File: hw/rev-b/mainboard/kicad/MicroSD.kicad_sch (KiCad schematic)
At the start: 5 parts, among them J25 MICRO_SD

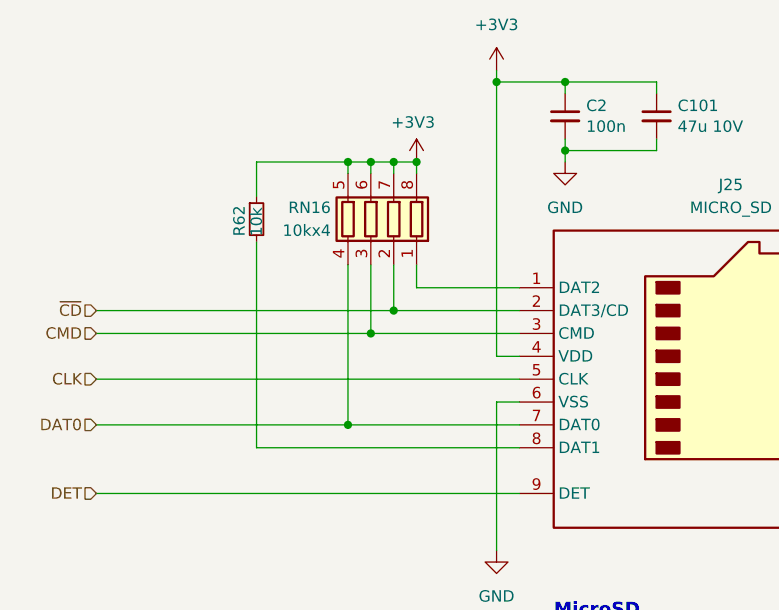
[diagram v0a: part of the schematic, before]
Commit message: hw: move USB-C for 8032SK (WIP)
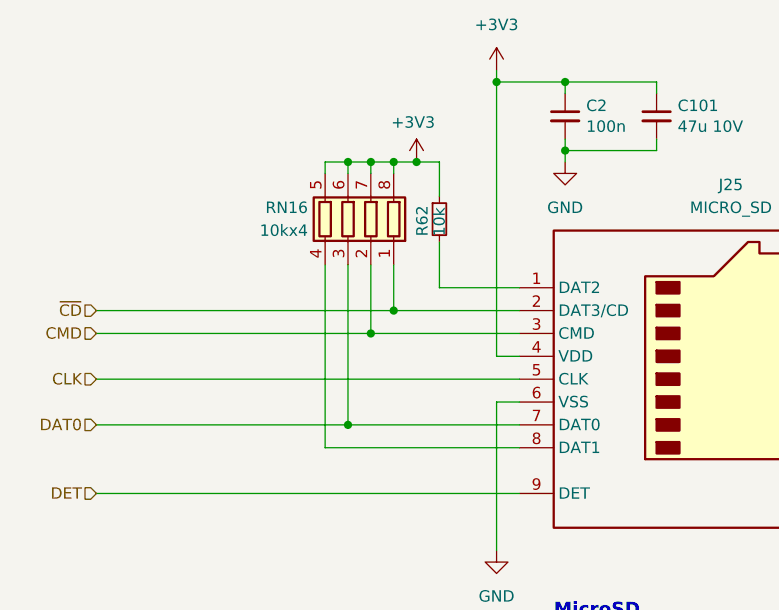
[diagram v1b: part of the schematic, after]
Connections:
- net CMD: now also RN16.2 (R2.1); no longer RN16.3 (R3.1)
- net DAT0: now also RN16.3 (R3.1); no longer RN16.4 (R4.1)
- net ~{CD}: now also RN16.1 (R1.1); no longer RN16.2 (R2.1)
- net at J25.1 (DAT2): now also R62.2; no longer RN16.1 (R1.1)
- net at J25.8 (DAT1): now also RN16.4 (R4.1); no longer R62.2
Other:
- moved on the sheet: R62, RN16
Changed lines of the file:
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@@
 	(wire
 		(pts
-			(xy 120.65 106.68) (xy 149.86 106.68)
-		)
-		(stroke
-			(width 0)
-			(type default)
-		)
-	)
-	(wire
-		(pts
-			(xy 120.65 74.93) (xy 130.81 74.93)
+			(xy 128.27 74.93) (xy 130.81 74.93)
 		)
 		(stroke
@@
 	(wire
 		(pts
+			(xy 128.27 74.93) (xy 128.27 76.2)
+		)
+		(stroke
+			(width 0)
+			(type default)
+		)
+	)
+	(wire
+		(pts
 			(xy 154.94 73.66) (xy 154.94 72.39)
 		)
@@
 	(wire
 		(pts
-			(xy 149.86 88.9) (xy 138.43 88.9)
+			(xy 149.86 88.9) (xy 140.97 88.9)
 		)
 		(stroke
@@
 	(wire
 		(pts
-			(xy 120.65 78.74) (xy 120.65 74.93)
+			(xy 128.27 106.68) (xy 149.86 106.68)
 		)
 		(stroke
@@
 	(wire
 		(pts
+			(xy 140.97 78.74) (xy 140.97 74.93)
+		)
+		(stroke
+			(width 0)
+			(type default)
+		)
+	)
+	(wire
+		(pts
 			(xy 135.89 86.36) (xy 135.89 91.44)
 		)
@@
 	(wire
 		(pts
-			(xy 138.43 74.93) (xy 138.43 76.2)
+			(xy 140.97 74.93) (xy 138.43 74.93)
 		)
 		(stroke
@@
 	(wire
 		(pts
+			(xy 140.97 83.82) (xy 140.97 88.9)
+		)
+		(stroke
+			(width 0)
+			(type default)
+		)
+	)
+	(wire
+		(pts
 			(xy 133.35 93.98) (xy 149.86 93.98)
 		)
@@
 	(wire
 		(pts
-			(xy 120.65 106.68) (xy 120.65 83.82)
-		)
-		(stroke
-			(width 0)
-			(type default)
-		)
-	)
-	(wire
-		(pts
 			(xy 102.87 93.98) (xy 133.35 93.98)
 		)
@@
 	(wire
 		(pts
-			(xy 138.43 86.36) (xy 138.43 88.9)
-		)
-		(stroke
-			(width 0)
-			(type default)
-		)
-	)
-	(wire
-		(pts
 			(xy 135.89 74.93) (xy 135.89 76.2)
 		)
@@
 		(pts
 			(xy 154.94 66.04) (xy 165.1 66.04)
+		)
+		(stroke
+			(width 0)
+			(type default)
+		)
+	)
+	(wire
+		(pts
+			(xy 128.27 86.36) (xy 128.27 106.68)
 		)
 		(stroke
@@
 	(symbol
 		(lib_id "Device:R_Pack04")
-		(at 133.35 81.28 0)
+		(at 130.81 81.28 0)
 		(mirror y)
 		(unit 1)
@@
 		(dnp no)
 		(property "Reference" "RN16"
-			(at 128.905 80.01 0)
+			(at 126.365 80.01 0)
 			(effects
 				(font
@@
 		)
 		(property "Value" "10kx4"
-			(at 128.905 82.55 0)
+			(at 126.365 82.55 0)
 			(effects
 				(font
@@
 		)
 		(property "Footprint" "Resistor_SMD:R_Array_Convex_4x0603"
-			(at 126.365 81.28 90)
+			(at 123.825 81.28 90)
 			(effects
 				(font
@@
 		)
 		(property "Datasheet" "https://www.lcsc.com/datasheet/lcsc_datasheet_2304140030_UNI-ROYAL-Uniroyal-Elec-4D03WGJ0103T5E_C29718.pdf"
-			(at 133.35 81.28 0)
+			(at 130.81 81.28 0)
 			(effects
 				(font
@@
 		)
 		(property "Description" "4 resistor network, parallel topology"
-			(at 133.35 81.28 0)
+			(at 130.81 81.28 0)
 			(effects
 				(font
@@
 		)
 		(property "LCSC" "C29718"
-			(at 133.35 81.28 0)
+			(at 130.81 81.28 0)
 			(effects
 				(font
@@
 	(symbol
 		(lib_id "Device:R_Small")
-		(at 120.65 81.28 0)
+		(at 140.97 81.28 0)
 		(unit 1)
 		(exclude_from_sim no)
@@
 		(dnp no)
 		(property "Reference" "R62"
-			(at 118.745 83.185 90)
+			(at 139.065 83.185 90)
 			(effects
 				(font
@@
 		)
 		(property "Value" "10k"
-			(at 120.65 83.185 90)
+			(at 140.97 83.185 90)
 			(effects
 				(font
@@
 		)
 		(property "Footprint" "Resistor_SMD:R_0402_1005Metric"
-			(at 120.65 81.28 0)
+			(at 140.97 81.28 0)
 			(effects
 				(font
@@
 		)
 		(property "Datasheet" "https://jlcpcb.com/api/file/downloadByFileSystemAccessId/8556212101498380288"
-			(at 120.65 81.28 0)
+			(at 140.97 81.28 0)
 			(effects
 				(font
@@
 		)
 		(property "Description" ""
-			(at 120.65 81.28 0)
+			(at 140.97 81.28 0)
 			(effects
 				(font
@@
 		)
 		(property "LCSC" "C25744"
-			(at 120.65 81.28 0)
-			(effects
-				(font
+			(at 140.97 81.28 0)
+			(effects
+				(font

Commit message: chore(hw): tidy and set ${REVISION} to "B"
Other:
- company: https://is.gd/6hpvh6 -> https://tinyurl.com/econopet-rev-b
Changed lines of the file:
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@@
 	(title_block
 		(title "EconoPET 40/8096")
-		(date "2026-02-27")
-		(rev "B")
-		(company "https://is.gd/6hpvh6")
+		(date "2026-08-25")
+		(rev "${REVISION}")
+		(company "https://tinyurl.com/econopet-rev-b")
 		(comment 1 "Unspecified resistors are 1% / 62.5mW")
 		(comment 2 "Unspecified capacitors are 25V")

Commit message: chore(hw): create production files
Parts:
- C101: LCSC C96123 -> (none); LCSC Part # (none) -> C96123
- C2: LCSC C307331 -> (none); LCSC Part # (none) -> C307331
- J25: FT Position Offset (none) -> -0.127,2.159; LCSC C393941 -> (none); LCSC Part # (none) -> C393941
- R62: LCSC C25744 -> (none); LCSC Part # (none) -> C25744
- RN16: LCSC C29718 -> (none); LCSC Part # (none) -> C29718
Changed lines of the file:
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@@
 			)
 		)
-		(property "LCSC" "C393941"
+		(property "LCSC Part #" "C393941"
+			(at 172.72 99.06 0)
+			(effects
+				(font
+					(size 1.27 1.27)
+				)
+				(hide yes)
+			)
+		)
+		(property "FT Position Offset" "-0.127,2.159"
+			(at 172.72 99.06 0)
+			(effects
+				(font
+					(size 1.27 1.27)
+				)
+				(hide yes)
+			)
+		)
+		(property "FT Rotation Offset" ""
 			(at 172.72 99.06 0)
 			(effects
@@
 			)
 		)
-		(property "LCSC" "C29718"
+		(property "LCSC Part #" "C29718"
+			(at 130.81 81.28 0)
+			(effects
+				(font
+					(size 1.27 1.27)
+				)
+				(hide yes)
+			)
+		)
+		(property "FT Position Offset" ""
+			(at 130.81 81.28 0)
+			(effects
+				(font
+					(size 1.27 1.27)
+				)
+				(hide yes)
+			)
+		)
+		(property "FT Rotation Offset" ""
 			(at 130.81 81.28 0)
 			(effects
@@
 			)
 		)
-		(property "LCSC" "C25744"
+		(property "LCSC Part #" "C25744"
+			(at 140.97 81.28 0)
+			(effects
+				(font
+					(size 1.27 1.27)
+				)
+				(hide yes)
+			)
+		)
+		(property "FT Position Offset" ""
+			(at 140.97 81.28 0)
+			(effects
+				(font
+					(size 1.27 1.27)
+				)
+				(hide yes)
+			)
+		)
+		(property "FT Rotation Offset" ""
 			(at 140.97 81.28 0)
 			(effects
@@
 			)
 		)
-		(property "LCSC" "C96123"
+		(property "LCSC Part #" "C96123"
+			(at 165.1 69.85 0)
+			(effects
+				(font
+					(size 1.27 1.27)
+				)
+				(hide yes)
+			)
+		)
+		(property "FT Position Offset" ""
+			(at 165.1 69.85 0)
+			(effects
+				(font
+					(size 1.27 1.27)
+				)
+				(hide yes)
+			)
+		)
+		(property "FT Rotation Offset" ""
 			(at 165.1 69.85 0)
 			(effects
@@
 			)
 		)
-		(property "LCSC" "C307331"
+		(property "LCSC Part #" "C307331"
 			(at 154.94 69.85 0)
 			(effects
+				(font
+					(size 1.27 1.27)
+				)
+				(hide yes)
+			)
+		)
+		(property "FT Position Offset" ""
+			(at 154.94 69.85 0)
+			(effects
+				(font
+					(size 1.27 1.27)
+				)
+				(hide yes)
+			)
+		)
+		(property "FT Rotation Offset" ""
+			(at 154.94 69.85 0)
+			(effects
